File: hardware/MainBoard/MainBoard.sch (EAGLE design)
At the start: 220 parts, among them J1 CON-71741-2184-BOT, J2 CON-71741-2184-TOP, J3 CON-FTSH-105-01-L-DV-K, J4 CON-ZX62R-B-5P, J5 CON-SMA, J6 CON-SMA, J7 CON-RJ45-J0G-0007NL, J8 SWITCH-CJS-1200-1200, M1 MOUNT-HOLE3.3, M2 MOUNT-HOLE3.3, M3 MOUNT-HOLE3.3, M4 MOUNT-HOLE3.3, M5 FIDUCIAL1X2, M6 FIDUCIAL1X2, M7 FIDUCIAL1X2, M8 FIDUCIAL1X2, Q1 MMBT3904, SW1 SWITCH-KSC-201J, SW2 SWITCH-KSC-201J, U1 A2F500M3G-FG256, U2 MAX19706-T4877-4, U3 MAX19706-T4877-4, U4 USBLC6-2SC6, U5 FT232HL, U6 DP83848C-VBH48A, U7 93LC56BT-OT, U8 DS1818-10-SOT-23, U9 LMV112, X1 FOX924B, X2 ECX-31B, X3 ASEM1-C, X5 ECX-42-120

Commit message: Starting add FPGA supply decoupling capacitors.
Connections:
- net NGPIO0: now also U1-EXTERNAL-MEMORY-CONTROLLER.EMC_DB[7]/GEB1/IO79PDB5V0; no longer U1-EXTERNAL-MEMORY-CONTROLLER.EMC_DB[6]/GEB0/IO79NDB5V0
- net SGPIO0: now also U1-EXTERNAL-MEMORY-CONTROLLER.EMC_DB[2]/IO77NDB5V0; no longer U1-EXTERNAL-MEMORY-CONTROLLER.EMC_DB[5]/GEA1/IO78PPB5V0
- net SGPIO1: now also U1-EXTERNAL-MEMORY-CONTROLLER.EMC_DB[5]/GEA1/IO78PPB5V0; no longer U1-EXTERNAL-MEMORY-CONTROLLER.EMC_DB[8]/GEC0/IO80NDB5V0
- net SGPIO2: now also U1-EXTERNAL-MEMORY-CONTROLLER.EMC_DB[8]/GEC0/IO80NDB5V0; no longer U1-EXTERNAL-MEMORY-CONTROLLER.EMC_DB[2]/IO77NDB5V0
- net SGPIO3: now also U1-EXTERNAL-MEMORY-CONTROLLER.EMC_DB[6]/GEB0/IO79NDB5V0; no longer U1-EXTERNAL-MEMORY-CONTROLLER.EMC_DB[7]/GEB1/IO79PDB5V0
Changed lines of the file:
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@@
 <rectangle x1="25.4" y1="71.12" x2="63.5" y2="91.44" layer="116"/>
 <rectangle x1="63.5" y1="71.12" x2="104.14" y2="81.28" layer="116"/>
+<rectangle x1="81.28" y1="2.54" x2="160.02" y2="33.02" layer="116"/>
+<rectangle x1="22.86" y1="129.54" x2="119.38" y2="175.26" layer="116"/>
 </plain>
 <instances>
@@
 <text x="134.62" y="62.23" size="1.778" layer="97">DAC LPF 4th pole (DNP)</text>
 <text x="175.26" y="111.76" size="1.778" layer="97">Check NPN BJT parameters</text>
-<text x="185.42" y="121.92" size="1.778" layer="97">NC</text>
+<text x="165.1" y="134.62" size="1.778" layer="97">NC</text>
 <text x="45.72" y="142.24" size="1.778" layer="97" rot="MR0">to North Bridge</text>
 <text x="180.34" y="86.36" size="1.778" layer="97">to North Bridge</text>
@@
 <rectangle x1="182.88" y1="38.1" x2="226.06" y2="73.66" layer="116"/>
 <rectangle x1="142.24" y1="99.06" x2="185.42" y2="119.38" layer="116"/>
+<text x="76.2" y="139.7" size="1.778" layer="97">NC</text>
+<text x="76.2" y="137.16" size="1.778" layer="97">NC</text>
+<text x="165.1" y="144.78" size="1.778" layer="97">NC</text>
+<text x="165.1" y="142.24" size="1.778" layer="97">NC</text>
+<text x="165.1" y="139.7" size="1.778" layer="97">NC</text>
+<text x="165.1" y="137.16" size="1.778" layer="97">NC</text>
+<text x="165.1" y="124.46" size="1.778" layer="97">NC</text>
+<rectangle x1="137.16" y1="91.44" x2="195.58" y2="99.06" layer="116"/>
+<rectangle x1="137.16" y1="119.38" x2="165.1" y2="127" layer="116"/>
+<rectangle x1="139.7" y1="134.62" x2="187.96" y2="147.32" layer="116"/>
+<rectangle x1="71.12" y1="137.16" x2="101.6" y2="149.86" layer="116"/>
+<rectangle x1="71.12" y1="124.46" x2="101.6" y2="137.16" layer="116"/>
+<rectangle x1="71.12" y1="111.76" x2="101.6" y2="124.46" layer="116"/>
+<rectangle x1="43.18" y1="78.74" x2="104.14" y2="104.14" layer="116"/>
+<rectangle x1="127" y1="83.82" x2="180.34" y2="91.44" layer="116"/>
 </plain>
 <instances>
@@
 <text x="58.42" y="104.14" size="50.8" layer="208">EXT</text>
 <text x="55.88" y="25.4" size="50.8" layer="208">AFE</text>
+<rectangle x1="10.16" y1="109.22" x2="48.26" y2="165.1" layer="116"/>
+<rectangle x1="83.82" y1="109.22" x2="119.38" y2="165.1" layer="116"/>
+<rectangle x1="7.62" y1="58.42" x2="60.96" y2="93.98" layer="116"/>
+<rectangle x1="12.7" y1="93.98" x2="48.26" y2="99.06" layer="116"/>
+<rectangle x1="129.54" y1="60.96" x2="167.64" y2="93.98" layer="116"/>
+<rectangle x1="129.54" y1="93.98" x2="167.64" y2="101.6" layer="116"/>
+<rectangle x1="127" y1="109.22" x2="165.1" y2="162.56" layer="116"/>
+<rectangle x1="200.66" y1="109.22" x2="233.68" y2="162.56" layer="116"/>
+<rectangle x1="193.04" y1="63.5" x2="231.14" y2="78.74" layer="116"/>
+<rectangle x1="193.04" y1="81.28" x2="233.68" y2="86.36" layer="116"/>
+<rectangle x1="193.04" y1="88.9" x2="228.6" y2="99.06" layer="116"/>
+<rectangle x1="73.66" y1="66.04" x2="114.3" y2="78.74" layer="116"/>
+<rectangle x1="73.66" y1="81.28" x2="111.76" y2="86.36" layer="116"/>
+<rectangle x1="73.66" y1="86.36" x2="111.76" y2="99.06" layer="116"/>
+<text x="6.985" y="106.045" size="1.778" layer="97">NC</text>
+<text x="6.985" y="103.505" size="1.778" layer="97">NC</text>
+<text x="123.825" y="103.505" size="1.778" layer="97">NC</text>
+<text x="123.825" y="106.045" size="1.778" layer="97">NC</text>
+<rectangle x1="5.08" y1="101.6" x2="48.26" y2="109.22" layer="116"/>
+<rectangle x1="127" y1="104.14" x2="165.1" y2="109.22" layer="116"/>
+<rectangle x1="73.66" y1="101.6" x2="116.84" y2="106.68" layer="116"/>
+<rectangle x1="190.5" y1="101.6" x2="231.14" y2="109.22" layer="116"/>
+<rectangle x1="12.7" y1="7.62" x2="144.78" y2="53.34" layer="116"/>
 </plain>
 <instances>
@@
 <rectangle x1="30.48" y1="132.08" x2="203.2" y2="170.18" layer="116"/>
 <rectangle x1="30.48" y1="91.44" x2="203.2" y2="127" layer="116"/>
+<rectangle x1="10.16" y1="15.24" x2="121.92" y2="68.58" layer="116"/>
 </plain>
 <instances>
@@
 </segment>
 </net>
-<net name="SGPIO3" class="0">
-<segment>
-<pinref part="U1" gate="-EXTERNAL-MEMORY-CONTROLLER" pin="EMC_DB[7]/GEB1/IO79PDB5V0"/>
-<wire x1="215.9" y1="137.16" x2="220.98" y2="137.16" width="0.1524" layer="91"/>
-<label x="223.52" y="137.16" size="1.778" layer="95"/>
-</segment>
-</net>
-<net name="SGPIO2" class="0">
-<segment>
-<pinref part="U1" gate="-EXTERNAL-MEMORY-CONTROLLER" pin="EMC_DB[2]/IO77NDB5V0"/>
-<wire x1="215.9" y1="149.86" x2="220.98" y2="149.86" width="0.1524" layer="91"/>
-<label x="223.52" y="149.86" size="1.778" layer="95"/>
-</segment>
-</net>
 <net name="NGPIO3" class="0">
 <segment>
@@
 <net name="SGPIO1" class="0">
 <segment>
-<pinref part="U1" gate="-EXTERNAL-MEMORY-CONTROLLER" pin="EMC_DB[8]/GEC0/IO80NDB5V0"/>
-<wire x1="215.9" y1="134.62" x2="220.98" y2="134.62" width="0.1524" layer="91"/>
-<label x="223.52" y="134.62" size="1.778" layer="95"/>
-</segment>
-</net>
-<net name="SGPIO0" class="0">
-<segment>
 <pinref part="U1" gate="-EXTERNAL-MEMORY-CONTROLLER" pin="EMC_DB[5]/GEA1/IO78PPB5V0"/>
 <wire x1="215.9" y1="142.24" x2="220.98" y2="142.24" width="0.1524" layer="91"/>
@@
 <net name="NGPIO0" class="0">
 <segment>
+<pinref part="U1" gate="-EXTERNAL-MEMORY-CONTROLLER" pin="EMC_DB[7]/GEB1/IO79PDB5V0"/>
+<wire x1="215.9" y1="137.16" x2="220.98" y2="137.16" width="0.1524" layer="91"/>
+<label x="223.52" y="137.16" size="1.778" layer="95"/>
+</segment>
+</net>
+<net name="SGPIO3" class="0">
+<segment>
 <pinref part="U1" gate="-EXTERNAL-MEMORY-CONTROLLER" pin="EMC_DB[6]/GEB0/IO79NDB5V0"/>
 <wire x1="215.9" y1="139.7" x2="220.98" y2="139.7" width="0.1524" layer="91"/>
@@
 </segment>
 </net>
+<net name="SGPIO0" class="0">
+<segment>
+<pinref part="U1" gate="-EXTERNAL-MEMORY-CONTROLLER" pin="EMC_DB[2]/IO77NDB5V0"/>
+<wire x1="215.9" y1="149.86" x2="220.98" y2="149.86" width="0.1524" layer="91"/>
+<label x="223.52" y="149.86" size="1.778" layer="95"/>
+</segment>
+</net>
+<net name="SGPIO2" class="0">
+<segment>
+<pinref part="U1" gate="-EXTERNAL-MEMORY-CONTROLLER" pin="EMC_DB[8]/GEC0/IO80NDB5V0"/>
+<wire x1="215.9" y1="134.62" x2="220.98" y2="134.62" width="0.1524" layer="91"/>
+<label x="223.52" y="134.62" size="1.778" layer="95"/>
+</segment>
+</net>
 </nets>
 </sheet>
@@
 <rectangle x1="215.9" y1="68.58" x2="223.52" y2="73.66" layer="98"/>
 <rectangle x1="203.2" y1="71.12" x2="233.68" y2="73.66" layer="116"/>
+<rectangle x1="22.86" y1="53.34" x2="88.9" y2="91.44" layer="116"/>
+<rectangle x1="20.32" y1="101.6" x2="88.9" y2="129.54" layer="116"/>
+<rectangle x1="20.32" y1="139.7" x2="88.9" y2="167.64" layer="116"/>
+<rectangle x1="170.18" y1="114.3" x2="223.52" y2="160.02" layer="116"/>
+<rectangle x1="30.48" y1="10.16" x2="45.72" y2="50.8" layer="116"/>
 </plain>
 <instances>
@@
 <pinref part="U1" gate="-UART" pin="UART_1_TXD/GPIO_28"/>
 <wire x1="50.8" y1="149.86" x2="38.1" y2="149.86" width="0.1524" layer="91"/>
+<label x="35.56" y="149.86" size="1.778" layer="95" rot="MR0"/>
 </segment>
 </net>
@@
 <pinref part="U1" gate="-UART" pin="UART_1_RXD/GPIO_29"/>
 <wire x1="50.8" y1="147.32" x2="38.1" y2="147.32" width="0.1524" layer="91"/>
+<label x="35.56" y="147.32" size="1.778" layer="95" rot="MR0"/>
 </segment>
 </net>
@@
 <text x="170.18" y="149.86" size="1.778" layer="98" rot="R90">Make it a differential GCL IN</text>
 <text x="233.68" y="149.86" size="1.778" layer="98" rot="R90">Make it a differential GCL IN</text>
+<rectangle x1="27.94" y1="127" x2="83.82" y2="162.56" layer="116"/>
+<rectangle x1="22.86" y1="76.2" x2="99.06" y2="119.38" layer="116"/>
+<rectangle x1="17.78" y1="53.34" x2="58.42" y2="66.04" layer="116"/>
+<rectangle x1="60.96" y1="55.88" x2="96.52" y2="68.58" layer="116"/>
+<rectangle x1="17.78" y1="17.78" x2="104.14" y2="30.48" layer="116"/>
 </plain>
 <instances>

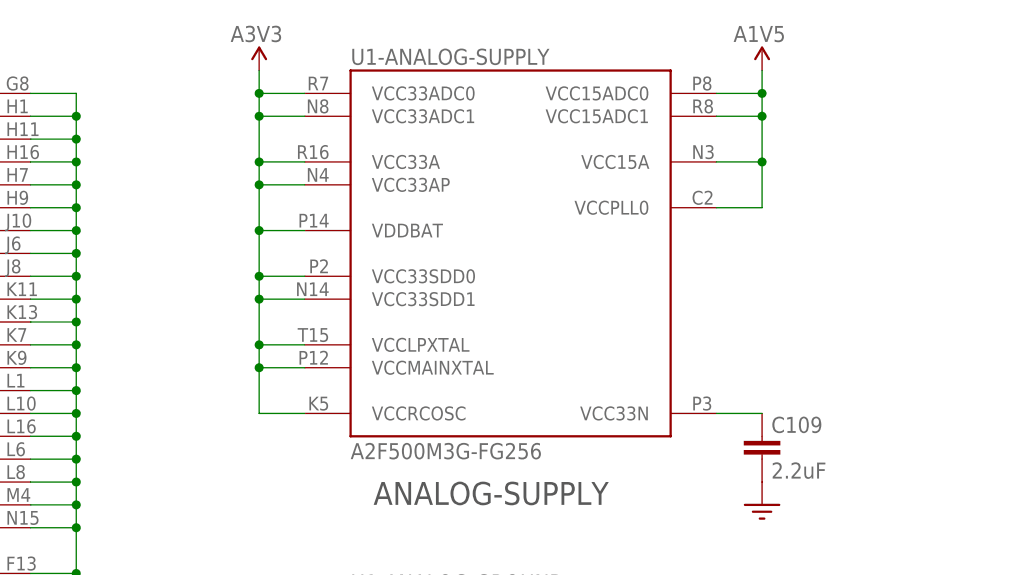
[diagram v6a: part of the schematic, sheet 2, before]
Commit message: 
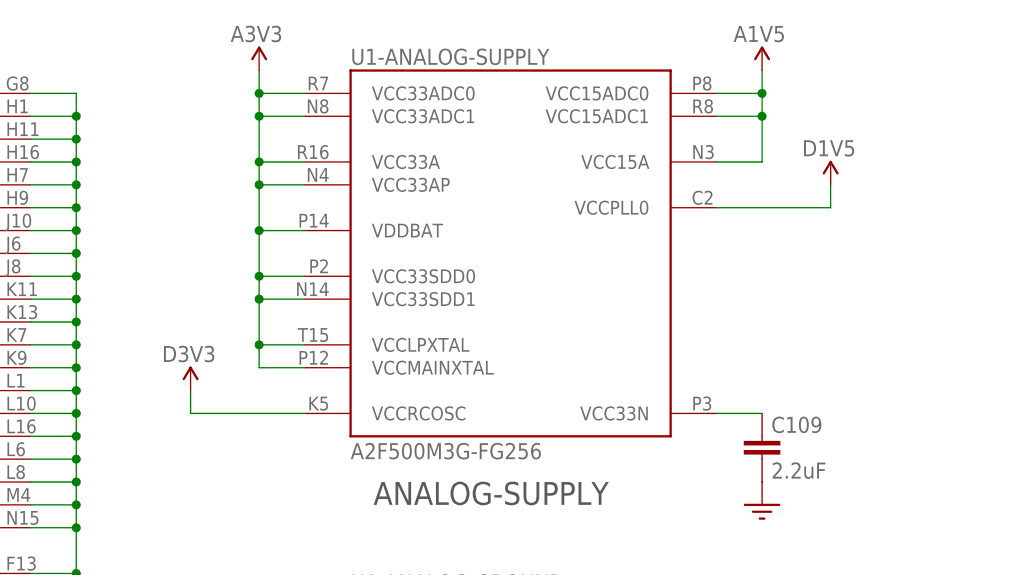
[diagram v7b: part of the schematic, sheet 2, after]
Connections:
- net A1V5: no longer U1-ANALOG-SUPPLY.VCCPLL0
- net A3V3: no longer U1-ANALOG-SUPPLY.VCCRCOSC
- net AGND: now also C3.2, C4.2
- net D1V5: now also U1-ANALOG-SUPPLY.VCCPLL0
- net D3V3: now also U1-ANALOG-SUPPLY.VCCRCOSC
- net DGND: no longer C3.2, C4.2
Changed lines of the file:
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@@
 <part name="PORT49" library="MainBoard" deviceset="PORT7" device=""/>
 <part name="PORT50" library="MainBoard" deviceset="PORT7" device=""/>
-<part name="U$22" library="MainBoard" deviceset="DGND" device=""/>
 <part name="C3" library="MainBoard" deviceset="C" device="0402" value="4pF"/>
 <part name="C4" library="MainBoard" deviceset="C" device="0402" value="4pF"/>
@@
 <part name="PORT361" library="MainBoard" deviceset="PORT5" device=""/>
 <part name="PORT362" library="MainBoard" deviceset="PORT5" device=""/>
+<part name="U$22" library="MainBoard" deviceset="AGND" device=""/>
+<part name="U$69" library="MainBoard" deviceset="D3V3" device=""/>
+<part name="U$80" library="MainBoard" deviceset="D1V5" device=""/>
 </parts>
 <sheets>
@@
 <instance part="U$11" gate="G$1" x="81.28" y="160.02"/>
 <instance part="U$105" gate="G$1" x="81.28" y="119.38"/>
+<instance part="U$69" gate="G$1" x="162.56" y="124.46"/>
+<instance part="U$80" gate="G$1" x="233.68" y="147.32"/>
 </instances>
 <busses>
@@
 <junction x="20.32" y="76.2"/>
 </segment>
+<segment>
+<pinref part="U1" gate="-ANALOG-SUPPLY" pin="VCCPLL0"/>
+<wire x1="220.98" y1="144.78" x2="233.68" y2="144.78" width="0.1524" layer="91"/>
+<wire x1="233.68" y1="144.78" x2="233.68" y2="147.32" width="0.1524" layer="91"/>
+<pinref part="U$80" gate="G$1" pin="D1V5"/>
+</segment>
 </net>
 <net name="D3V3" class="0">
@@
 <wire x1="76.2" y1="116.84" x2="81.28" y2="116.84" width="0.1524" layer="91"/>
 <pinref part="U$105" gate="G$1" pin="D3V3"/>
+</segment>
+<segment>
+<pinref part="U1" gate="-ANALOG-SUPPLY" pin="VCCRCOSC"/>
+<wire x1="175.26" y1="121.92" x2="162.56" y2="121.92" width="0.1524" layer="91"/>
+<wire x1="162.56" y1="121.92" x2="162.56" y2="124.46" width="0.1524" layer="91"/>
+<pinref part="U$69" gate="G$1" pin="D3V3"/>
 </segment>
 </net>
@@
 <junction x="226.06" y="154.94"/>
 <junction x="226.06" y="157.48"/>
-<pinref part="U1" gate="-ANALOG-SUPPLY" pin="VCCPLL0"/>
-<wire x1="220.98" y1="144.78" x2="226.06" y2="144.78" width="0.1524" layer="91"/>
-<wire x1="226.06" y1="144.78" x2="226.06" y2="149.86" width="0.1524" layer="91"/>
-<junction x="226.06" y="149.86"/>
 </segment>
 </net>
@@
 <segment>
 <pinref part="U$111" gate="G$1" pin="A3V3"/>
-<wire x1="170.18" y1="121.92" x2="170.18" y2="127" width="0.1524" layer="91"/>
-<pinref part="U1" gate="-ANALOG-SUPPLY" pin="VCCRCOSC"/>
 <wire x1="170.18" y1="127" x2="170.18" y2="129.54" width="0.1524" layer="91"/>
 <wire x1="170.18" y1="129.54" x2="170.18" y2="134.62" width="0.1524" layer="91"/>
@@
 <wire x1="170.18" y1="154.94" x2="170.18" y2="157.48" width="0.1524" layer="91"/>
 <wire x1="170.18" y1="157.48" x2="170.18" y2="160.02" width="0.1524" layer="91"/>
-<wire x1="175.26" y1="121.92" x2="170.18" y2="121.92" width="0.1524" layer="91"/>
 <pinref part="U1" gate="-ANALOG-SUPPLY" pin="VDDBAT"/>
 <wire x1="175.26" y1="142.24" x2="170.18" y2="142.24" width="0.1524" layer="91"/>
@@
 <pinref part="U1" gate="-ANALOG-SUPPLY" pin="VCCMAINXTAL"/>
 <wire x1="175.26" y1="127" x2="170.18" y2="127" width="0.1524" layer="91"/>
-<junction x="170.18" y="127"/>
 <junction x="170.18" y="129.54"/>
 <junction x="170.18" y="134.62"/>
@@
 <instance part="X1" gate="G$1" x="48.26" y="43.18"/>
 <instance part="X2" gate="G$1" x="38.1" y="124.46" rot="R90"/>
-<instance part="U$22" gate="G$1" x="25.4" y="114.3"/>
 <instance part="C3" gate="G$1" x="33.02" y="129.54" rot="R270"/>
 <instance part="C4" gate="G$1" x="33.02" y="119.38" rot="R270"/>
@@
 <instance part="PORT361" gate="G$1" x="200.66" y="73.66" rot="R90"/>
 <instance part="PORT362" gate="G$1" x="220.98" y="73.66" rot="R90"/>
+<instance part="U$22" gate="G$1" x="25.4" y="114.3"/>
 </instances>
 <busses>
@@
 </net>
 <net name="DGND" class="0">
-<segment>
-<pinref part="U$22" gate="G$1" pin="DGND"/>
-<wire x1="25.4" y1="129.54" x2="25.4" y2="119.38" width="0.1524" layer="91"/>
-<wire x1="25.4" y1="119.38" x2="25.4" y2="116.84" width="0.1524" layer="91"/>
-<pinref part="C3" gate="G$1" pin="2"/>
-<wire x1="27.94" y1="129.54" x2="25.4" y2="129.54" width="0.1524" layer="91"/>
-<pinref part="C4" gate="G$1" pin="2"/>
-<wire x1="27.94" y1="119.38" x2="25.4" y2="119.38" width="0.1524" layer="91"/>
-</segment>
 <segment>
 <pinref part="U$114" gate="G$1" pin="DGND"/>
@@
 </segment>
 </net>
+<net name="AGND" class="0">
+<segment>
+<wire x1="25.4" y1="129.54" x2="25.4" y2="119.38" width="0.1524" layer="91"/>
+<wire x1="25.4" y1="119.38" x2="25.4" y2="116.84" width="0.1524" layer="91"/>
+<pinref part="C3" gate="G$1" pin="2"/>
+<wire x1="27.94" y1="129.54" x2="25.4" y2="129.54" width="0.1524" layer="91"/>
+<pinref part="C4" gate="G$1" pin="2"/>
+<wire x1="27.94" y1="119.38" x2="25.4" y2="119.38" width="0.1524" layer="91"/>
+<pinref part="U$22" gate="G$1" pin="AGND"/>
+</segment>
+</net>
